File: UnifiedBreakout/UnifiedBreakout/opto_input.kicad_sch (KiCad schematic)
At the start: 5 parts, among them J17 RJ14, U3 4N35

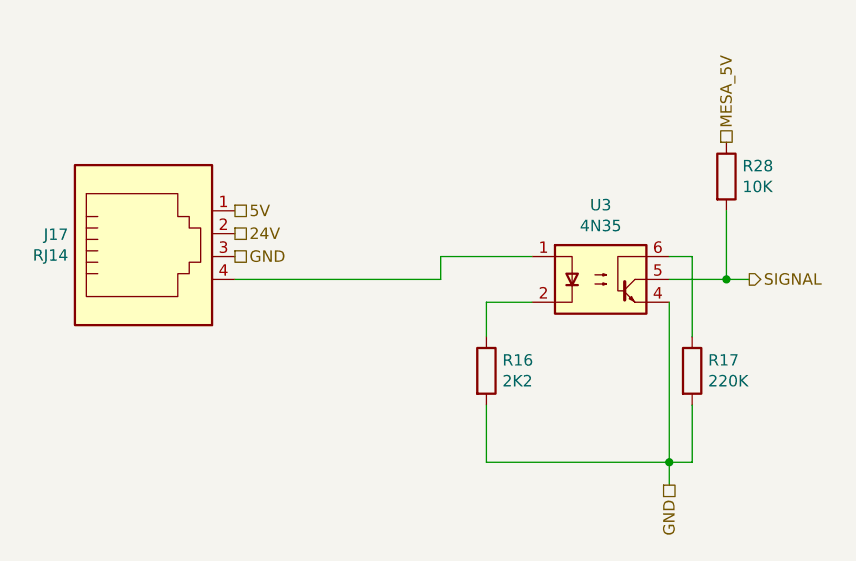
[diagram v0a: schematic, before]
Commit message: Upgrade to new KiCAD version
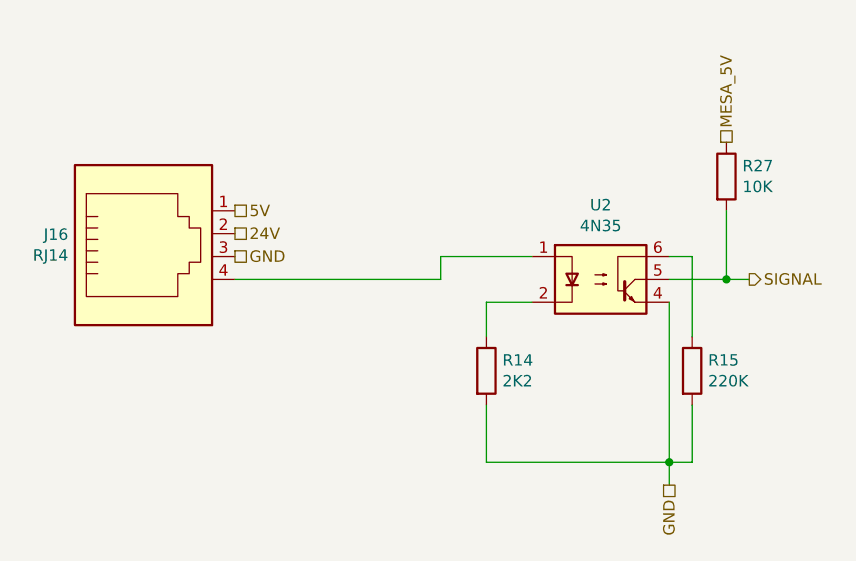
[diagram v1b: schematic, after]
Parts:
- renumbered J17 to J16, R16 to R14, R17 to R15, R28 to R27, U3 to U2
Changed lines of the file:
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@@
-(kicad_sch (version 20210126) (generator eeschema)
+(kicad_sch (version 20211123) (generator eeschema)
   (paper "A4")
-  (junction (at 153.67 109.22) (diameter 0.9144) (color 0 0 0 0))
-  (junction (at 160.02 88.9) (diameter 0.9144) (color 0 0 0 0))
-  (wire (pts (xy 105.41 88.9) (xy 128.27 88.9))
+  (junction (at 160.02 88.9) (diameter 0.9144) (color 0 0 0 0)
+  )
+  (junction (at 153.67 109.22) (diameter 0.9144) (color 0 0 0 0)
+  )
+  (wire (pts (xy 153.67 88.9) (xy 160.02 88.9))
     (stroke (width 0) (type solid) (color 0 0 0 0))
   )
-  (wire (pts (xy 128.27 86.36) (xy 138.43 86.36))
+  (wire (pts (xy 133.35 91.44) (xy 133.35 95.25))
+    (stroke (width 0) (type solid) (color 0 0 0 0))
+  )
+  (wire (pts (xy 156.21 86.36) (xy 156.21 95.25))
+    (stroke (width 0) (type solid) (color 0 0 0 0))
+  )
+  (wire (pts (xy 160.02 88.9) (xy 162.56 88.9))
     (stroke (width 0) (type solid) (color 0 0 0 0))
   )
@@
     (stroke (width 0) (type solid) (color 0 0 0 0))
   )
-  (wire (pts (xy 133.35 91.44) (xy 133.35 95.25))
+  (wire (pts (xy 138.43 91.44) (xy 133.35 91.44))
+    (stroke (width 0) (type solid) (color 0 0 0 0))
+  )
+  (wire (pts (xy 160.02 81.28) (xy 160.02 88.9))
+    (stroke (width 0) (type solid) (color 0 0 0 0))
+  )
+  (wire (pts (xy 156.21 102.87) (xy 156.21 109.22))
+    (stroke (width 0) (type solid) (color 0 0 0 0))
+  )
+  (wire (pts (xy 153.67 91.44) (xy 153.67 109.22))
     (stroke (width 0) (type solid) (color 0 0 0 0))
   )
@@
     (stroke (width 0) (type solid) (color 0 0 0 0))
   )
-  (wire (pts (xy 138.43 91.44) (xy 133.35 91.44))
-    (stroke (width 0) (type solid) (color 0 0 0 0))
-  )
-  (wire (pts (xy 153.67 86.36) (xy 156.21 86.36))
-    (stroke (width 0) (type solid) (color 0 0 0 0))
-  )
-  (wire (pts (xy 153.67 88.9) (xy 160.02 88.9))
-    (stroke (width 0) (type solid) (color 0 0 0 0))
-  )
-  (wire (pts (xy 153.67 91.44) (xy 153.67 109.22))
+  (wire (pts (xy 128.27 86.36) (xy 138.43 86.36))
     (stroke (width 0) (type solid) (color 0 0 0 0))
   )
@@
     (stroke (width 0) (type solid) (color 0 0 0 0))
   )
-  (wire (pts (xy 156.21 86.36) (xy 156.21 95.25))
-    (stroke (width 0) (type solid) (color 0 0 0 0))
-  )
-  (wire (pts (xy 156.21 102.87) (xy 156.21 109.22))
-    (stroke (width 0) (type solid) (color 0 0 0 0))
-  )
   (wire (pts (xy 156.21 109.22) (xy 153.67 109.22))
     (stroke (width 0) (type solid) (color 0 0 0 0))
   )
-  (wire (pts (xy 160.02 81.28) (xy 160.02 88.9))
+  (wire (pts (xy 153.67 86.36) (xy 156.21 86.36))
     (stroke (width 0) (type solid) (color 0 0 0 0))
   )
-  (wire (pts (xy 160.02 88.9) (xy 162.56 88.9))
+  (wire (pts (xy 105.41 88.9) (xy 128.27 88.9))
     (stroke (width 0) (type solid) (color 0 0 0 0))
+  )
+  (hierarchical_label "SIGNAL" (shape output) (at 162.56 88.9 0)
+    (effects (font (size 1.27 1.27)) (justify left))
+  )
+  (hierarchical_label "GND" (shape passive) (at 153.67 111.76 270)
+    (effects (font (size 1.27 1.27)) (justify right))
   )
   (hierarchical_label "5V" (shape passive) (at 105.41 81.28 0)
@@
     (effects (font (size 1.27 1.27)) (justify left))
   )
-  (hierarchical_label "GND" (shape passive) (at 153.67 111.76 270)
-    (effects (font (size 1.27 1.27)) (justify right))
-  )
   (hierarchical_label "MESA_5V" (shape passive) (at 160.02 73.66 90)
     (effects (font (size 1.27 1.27)) (justify left))
   )
-  (hierarchical_label "SIGNAL" (shape output) (at 162.56 88.9 0)
-    (effects (font (size 1.27 1.27)) (justify left))
+  (symbol (lib_id "UnifiedBreakout-rescue:R-Device") (at 160.02 77.47 0) (unit 1)
+    (in_bom yes) (on_board yes)
+    (property "Reference" "R27" (id 0) (at 161.798 76.3016 0)
+      (effects (font (size 1.27 1.27)) (justify left))
+    )
+    (property "Value" "10K" (id 1) (at 161.798 78.613 0)
+      (effects (font (size 1.27 1.27)) (justify left))
+    )
+    (property "Footprint" "Resistor_THT:R_Axial_DIN0207_L6.3mm_D2.5mm_P7.62mm_Horizontal" (id 2) (at 158.242 77.47 90)
+      (effects (font (size 1.27 1.27)) hide)
+    )
+    (property "Datasheet" "~" (id 3) (at 160.02 77.47 0)
+      (effects (font (size 1.27 1.27)) hide)
+    )
+    (property "MPN" "CFR-25JB-52-10K " (id 4) (at 160.02 77.47 0)
+      (effects (font (size 1.27 1.27)) hide)
+    )
+    (property "Manufacturer" "Yageo" (id 5) (at 160.02 77.47 0)
+      (effects (font (size 1.27 1.27)) hide)
+    )
+    (pin "1")
+    (pin "2")
   )
-  (symbol (lib_id "UnifiedBreakout-rescue:R-Device") (at 133.35 99.06 0)
+  (symbol (lib_id "UnifiedBreakout-rescue:4N35-Isolator") (at 146.05 88.9 0) (unit 1)
     (in_bom yes) (on_board yes)
-    (property "Reference" "R16" (id 0) (at 135.128 97.8916 0)
+    (property "Reference" "U2" (id 0) (at 146.05 80.645 0))
+    (property "Value" "4N35" (id 1) (at 146.05 82.9564 0))
+    (property "Footprint" "Package_DIP:DIP-6_W7.62mm" (id 2) (at 140.97 93.98 0)
+      (effects (font (size 1.27 1.27) italic) (justify left) hide)
+    )
+    (property "Datasheet" "https://www.vishay.com/docs/81181/4n35.pdf" (id 3) (at 146.05 88.9 0)
+      (effects (font (size 1.27 1.27)) (justify left) hide)
+    )
+    (property "MPN" "4N35" (id 4) (at 146.05 88.9 0)
+      (effects (font (size 1.27 1.27)) hide)
+    )
+    (property "Manufacturer" "Vishay" (id 5) (at 146.05 88.9 0)
+      (effects (font (size 1.27 1.27)) hide)
+    )
+    (pin "1")
+    (pin "2")
+    (pin "3")
+    (pin "4")
+    (pin "5")
+    (pin "6")
+  )
+  (symbol (lib_id "UnifiedBreakout-rescue:R-Device") (at 133.35 99.06 0) (unit 1)
+    (in_bom yes) (on_board yes)
+    (property "Reference" "R14" (id 0) (at 135.128 97.8916 0)
       (effects (font (size 1.27 1.27)) (justify left))
     )
@@
     (pin "2")
   )
-  (symbol (lib_id "UnifiedBreakout-rescue:R-Device") (at 156.21 99.06 0)
+  (symbol (lib_id "UnifiedBreakout-rescue:RJ14-Connector") (at 95.25 83.82 0) (mirror x) (unit 1)
     (in_bom yes) (on_board yes)
-    (property "Reference" "R17" (id 0) (at 157.988 97.8916 0)
-      (effects (font (size 1.27 1.27)) (justify left))
-    )
-    (property "Value" "220K" (id 1) (at 157.988 100.203 0)
-      (effects (font (size 1.27 1.27)) (justify left))
-    )
-    (property "Footprint" "Resistor_THT:R_Axial_DIN0207_L6.3mm_D2.5mm_P7.62mm_Horizontal" (id 2) (at 154.432 99.06 90)
-      (effects (font (size 1.27 1.27)) hide)
-    )
-    (property "Datasheet" "~" (id 3) (at 156.21 99.06 0)
-      (effects (font (size 1.27 1.27)) hide)
-    )
-    (property "MPN" "CFR-25JB-52-220K" (id 4) (at 156.21 99.06 0)
-      (effects (font (size 1.27 1.27)) hide)
-    )
-    (property "Manufacturer" "Yageo" (id 5) (at 156.21 99.06 0)
-      (effects (font (size 1.27 1.27)) hide)
-    )
-    (pin "1")
-    (pin "2")
-  )
-  (symbol (lib_id "UnifiedBreakout-rescue:R-Device") (at 160.02 77.47 0)
-    (in_bom yes) (on_board yes)
-    (property "Reference" "R28" (id 0) (at 161.798 76.3016 0)
-      (effects (font (size 1.27 1.27)) (justify left))
-    )
-    (property "Value" "10K" (id 1) (at 161.798 78.613 0)
-      (effects (font (size 1.27 1.27)) (justify left))
-    )
-    (property "Footprint" "Resistor_THT:R_Axial_DIN0207_L6.3mm_D2.5mm_P7.62mm_Horizontal" (id 2) (at 158.242 77.47 90)
-      (effects (font (size 1.27 1.27)) hide)
-    )
-    (property "Datasheet" "~" (id 3) (at 160.02 77.47 0)
-      (effects (font (size 1.27 1.27)) hide)
-    )
-    (property "MPN" "CFR-25JB-52-10K " (id 4) (at 160.02 77.47 0)
-      (effects (font (size 1.27 1.27)) hide)
-    )
-    (property "Manufacturer" "Yageo" (id 5) (at 160.02 77.47 0)
-      (effects (font (size 1.27 1.27)) hide)
-    )
-    (pin "1")
-    (pin "2")
-  )
-  (symbol (lib_id "UnifiedBreakout-rescue:4N35-Isolator") (at 146.05 88.9 0)
-    (in_bom yes) (on_board yes)
-    (property "Reference" "U3" (id 0) (at 146.05 80.645 0))
-    (property "Value" "4N35" (id 1) (at 146.05 82.9564 0))
-    (property "Footprint" "Package_DIP:DIP-6_W7.62mm" (id 2) (at 140.97 93.98 0)
-      (effects (font (size 1.27 1.27) italic) (justify left) hide)
-    )
-    (property "Datasheet" "https://www.vishay.com/docs/81181/4n35.pdf" (id 3) (at 146.05 88.9 0)
-      (effects (font (size 1.27 1.27)) (justify left) hide)
-    )
-    (property "MPN" "4N35" (id 4) (at 146.05 88.9 0)
-      (effects (font (size 1.27 1.27)) hide)
-    )
-    (property "Manufacturer" "Vishay" (id 5) (at 146.05 88.9 0)
-      (effects (font (size 1.27 1.27)) hide)
-    )
-    (pin "1")
-    (pin "2")
-    (pin "3")
-    (pin "4")
-    (pin "5")
-    (pin "6")
-  )
-  (symbol (lib_id "UnifiedBreakout-rescue:RJ14-Connector") (at 95.25 83.82 0) (mirror x)
-    (in_bom yes) (on_board yes)
-    (property "Reference" "J17" (id 0) (at 86.8934 83.9216 0)
+    (property "Reference" "J16" (id 0) (at 86.8934 83.9216 0)
       (effects (font (size 1.27 1.27)) (justify right))
     )
@@
     (pin "4")
   )
+  (symbol (lib_id "UnifiedBreakout-rescue:R-Device") (at 156.21 99.06 0) (unit 1)
+    (in_bom yes) (on_board yes)
+    (property "Reference" "R15" (id 0) (at 157.988 97.8916 0)
+      (effects (font (size 1.27 1.27)) (justify left))
+    )
+    (property "Value" "220K" (id 1) (at 157.988 100.203 0)
+      (effects (font (size 1.27 1.27)) (justify left))
+    )
+    (property "Footprint" "Resistor_THT:R_Axial_DIN0207_L6.3mm_D2.5mm_P7.62mm_Horizontal" (id 2) (at 154.432 99.06 90)
+      (effects (font (size 1.27 1.27)) hide)
+    )
+    (property "Datasheet" "~" (id 3) (at 156.21 99.06 0)
+      (effects (font (size 1.27 1.27)) hide)
+    )
+    (property "MPN" "CFR-25JB-52-220K" (id 4) (at 156.21 99.06 0)
+      (effects (font (size 1.27 1.27)) hide)
+    )
+    (property "Manufacturer" "Yageo" (id 5) (at 156.21 99.06 0)
+      (effects (font (size 1.27 1.27)) hide)
+    )
+    (pin "1")
+    (pin "2")
+  )
 )

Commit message: WIP updating breakout for electrical enclosure
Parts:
- removed J16: RJ14, Wurth:615004141121, symbol UnifiedBreakout-rescue:RJ14-Connector
- R14, R15, R27: symbol UnifiedBreakout-rescue:R-Device -> Device:R
- U2: symbol UnifiedBreakout-rescue:4N35-Isolator -> Isolator:4N35
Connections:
- net INPUT: now reaches U2.1

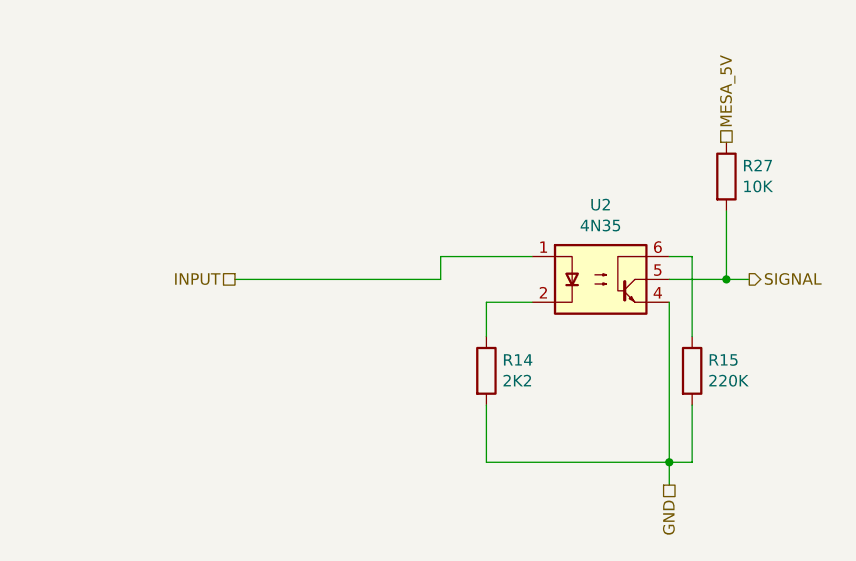
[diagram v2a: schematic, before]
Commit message: Update IO and opto
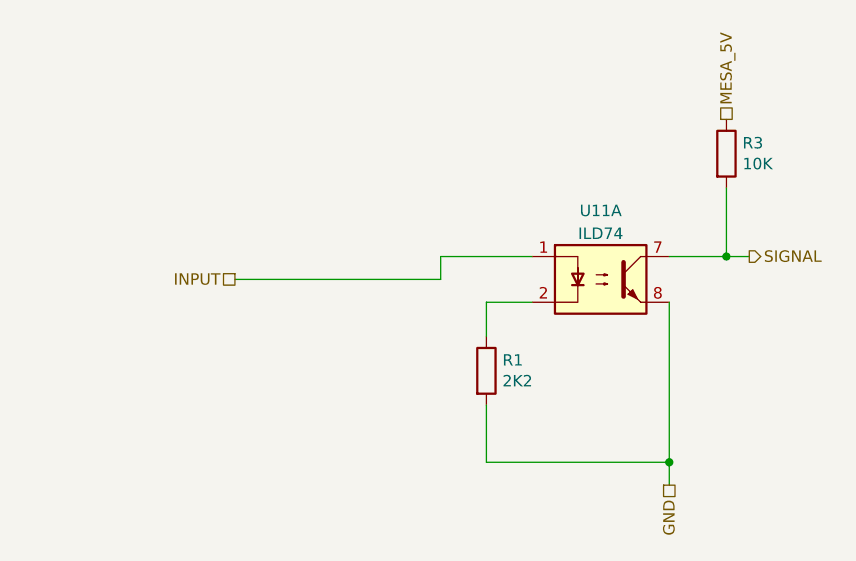
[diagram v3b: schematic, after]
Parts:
- removed R15: 220K, Resistor_THT:R_Axial_DIN0207_L6.3mm_D2.5mm_P7.62mm_Horizontal, symbol Device:R
- removed U2: 4N35, Package_DIP:DIP-6_W7.62mm, symbol Isolator:4N35
- added U11: ILD74, Package_DIP:DIP-8_W7.62mm_LongPads, symbol Isolator:ILD74
- renumbered R14 to R1, R27 to R3
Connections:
- net GND: now also U11.8
- net INPUT: now also U11.1
- net SIGNAL: now also U11.7
- net at R1.1: now also U11.2
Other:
- moved on the sheet: R3

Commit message: Started some layout
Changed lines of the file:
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@@
   (junction (at 160.02 86.36) (diameter 0.9144) (color 0 0 0 0)
   )
-  (junction (at 153.67 109.22) (diameter 0.9144) (color 0 0 0 0)
-  )
   (wire (pts (xy 153.67 86.36) (xy 160.02 86.36))
     (stroke (width 0) (type solid))
@@
     (stroke (width 0) (type solid))
   )
-  (wire (pts (xy 153.67 91.44) (xy 153.67 109.22))
+  (wire (pts (xy 153.67 91.44) (xy 153.67 111.76))
     (stroke (width 0) (type solid))
   )
@@
   )
   (wire (pts (xy 128.27 86.36) (xy 138.43 86.36))
-    (stroke (width 0) (type solid))
-  )
-  (wire (pts (xy 153.67 109.22) (xy 133.35 109.22))
-    (stroke (width 0) (type solid))
-  )
-  (wire (pts (xy 153.67 109.22) (xy 153.67 111.76))
     (stroke (width 0) (type solid))
   )
@@
         )
       )
+    )
+  )
+  (symbol (lib_id "power:GND") (at 133.35 109.22 0) (unit 1)
+    (in_bom yes) (on_board yes) (dnp no) (fields_autoplaced)
+    (property "Reference" "#PWR045" (at 133.35 114.3 0)
+      (effects (font (size 1.27 1.27)) hide)
+    )
+    (property "Value" "GNDPWR" (at 133.223 114.3 0)
+      (effects (font (size 1.27 1.27)))
+    )
+    (property "Footprint" "" (at 133.35 109.22 0)
+      (effects (font (size 1.27 1.27)) hide)
+    )
+    (property "Datasheet" "" (at 133.35 109.22 0)
+      (effects (font (size 1.27 1.27)) hide)
+    )
+    (pin "1")
+    (instances
+      (project "UnifiedBreakout"
+        (path "/e63e39d7-6ac0-4ffd-8aa3-1841a4541b55/00000000-0000-0000-0000-00005ea83ccc"
+          (reference "#PWR045") (unit 1)
+        )
+        (path "/e63e39d7-6ac0-4ffd-8aa3-1841a4541b55/00000000-0000-0000-0000-00005ea623ae"
+          (reference "#PWR043") (unit 1)
+        )
+        (path "/e63e39d7-6ac0-4ffd-8aa3-1841a4541b55/00000000-0000-0000-0000-00005ea86618"
+          (reference "#PWR044") (unit 1)
+        )
+        (path "/e63e39d7-6ac0-4ffd-8aa3-1841a4541b55/00000000-0000-0000-0000-00005ea816c6"
+          (reference "#PWR046") (unit 1)
+        )
+        (path "/e63e39d7-6ac0-4ffd-8aa3-1841a4541b55/00000000-0000-0000-0000-00005ea7f263"
+          (reference "#PWR047") (unit 1)
+        )
+        (path "/e63e39d7-6ac0-4ffd-8aa3-1841a4541b55/a961b421-d2a6-477a-a4b0-5977252d73f9"
+          (reference "#PWR048") (unit 1)
+        )
+      )

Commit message: Some layout
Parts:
- renumbered R3 to R2, U11 to U1
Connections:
- net GND: now also U1.5; no longer U1.8
- net INPUT: now also U1.4; no longer U1.1
- net SIGNAL: now also U1.6; no longer U1.7
- net at R1.1: now also U1.3; no longer U1.2
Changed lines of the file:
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@@
   (symbol (lib_id "Device:R") (at 160.02 74.93 0) (unit 1)
     (in_bom yes) (on_board yes) (dnp no)
-    (property "Reference" "R3" (at 161.798 73.7616 0)
+    (property "Reference" "R2" (at 161.798 73.7616 0)
       (effects (font (size 1.27 1.27)) (justify left))
     )
@@
       (project "UnifiedBreakout"
         (path "/e63e39d7-6ac0-4ffd-8aa3-1841a4541b55/00000000-0000-0000-0000-00005ea623ae"
-          (reference "R3") (unit 1)
+          (reference "R2") (unit 1)
         )
         (path "/e63e39d7-6ac0-4ffd-8aa3-1841a4541b55/00000000-0000-0000-0000-00005ea7f263"
-          (reference "R15") (unit 1)
+          (reference "R10") (unit 1)
         )
         (path "/e63e39d7-6ac0-4ffd-8aa3-1841a4541b55/00000000-0000-0000-0000-00005ea816c6"
-          (reference "R12") (unit 1)
+          (reference "R8") (unit 1)
         )
         (path "/e63e39d7-6ac0-4ffd-8aa3-1841a4541b55/00000000-0000-0000-0000-00005ea83ccc"
-          (reference "R9") (unit 1)
+          (reference "R6") (unit 1)
         )
         (path "/e63e39d7-6ac0-4ffd-8aa3-1841a4541b55/00000000-0000-0000-0000-00005ea86618"
-          (reference "R6") (unit 1)
+          (reference "R4") (unit 1)
         )
         (path "/e63e39d7-6ac0-4ffd-8aa3-1841a4541b55/a961b421-d2a6-477a-a4b0-5977252d73f9"
-          (reference "R25") (unit 1)
+          (reference "R20") (unit 1)
         )
       )
@@
         )
         (path "/e63e39d7-6ac0-4ffd-8aa3-1841a4541b55/00000000-0000-0000-0000-00005ea7f263"
-          (reference "R13") (unit 1)
+          (reference "R9") (unit 1)
         )
         (path "/e63e39d7-6ac0-4ffd-8aa3-1841a4541b55/00000000-0000-0000-0000-00005ea816c6"
-          (reference "R10") (unit 1)
+          (reference "R7") (unit 1)
         )
         (path "/e63e39d7-6ac0-4ffd-8aa3-1841a4541b55/00000000-0000-0000-0000-00005ea83ccc"
-          (reference "R7") (unit 1)
+          (reference "R5") (unit 1)
         )
         (path "/e63e39d7-6ac0-4ffd-8aa3-1841a4541b55/00000000-0000-0000-0000-00005ea86618"
-          (reference "R4") (unit 1)
+          (reference "R3") (unit 1)
         )
         (path "/e63e39d7-6ac0-4ffd-8aa3-1841a4541b55/a961b421-d2a6-477a-a4b0-5977252d73f9"
-          (reference "R23") (unit 1)
+          (reference "R19") (unit 1)
         )
       )
     )
   )
-  (symbol (lib_id "Isolator:ILD74") (at 146.05 88.9 0) (unit 1)
+  (symbol (lib_id "Isolator:ILD74") (at 146.05 88.9 0) (unit 2)
     (in_bom yes) (on_board yes) (dnp no) (fields_autoplaced)
-    (property "Reference" "U11" (at 146.05 81.28 0)
+    (property "Reference" "U1" (at 146.05 81.28 0)
       (effects (font (size 1.27 1.27)))
     )
@@
       (project "UnifiedBreakout"
         (path "/e63e39d7-6ac0-4ffd-8aa3-1841a4541b55/00000000-0000-0000-0000-00005ea623ae"
-          (reference "U11") (unit 1)
+          (reference "U1") (unit 2)
         )
         (path "/e63e39d7-6ac0-4ffd-8aa3-1841a4541b55/00000000-0000-0000-0000-00005ea86618"
-          (reference "U13") (unit 2)
+          (reference "U1") (unit 1)
         )
         (path "/e63e39d7-6ac0-4ffd-8aa3-1841a4541b55/00000000-0000-0000-0000-00005ea83ccc"
-          (reference "U12") (unit 2)
+          (reference "U2") (unit 1)
         )
         (path "/e63e39d7-6ac0-4ffd-8aa3-1841a4541b55/00000000-0000-0000-0000-00005ea816c6"
-          (reference "U12") (unit 1)
+          (reference "U3") (unit 2)
         )
         (path "/e63e39d7-6ac0-4ffd-8aa3-1841a4541b55/00000000-0000-0000-0000-00005ea7f263"
-          (reference "U11") (unit 2)
+          (reference "U3") (unit 1)
         )
         (path "/e63e39d7-6ac0-4ffd-8aa3-1841a4541b55/a961b421-d2a6-477a-a4b0-5977252d73f9"
-          (reference "U13") (unit 1)
+          (reference "U2") (unit 2)
         )
       )
@@
   (symbol (lib_id "power:GND") (at 133.35 109.22 0) (unit 1)
     (in_bom yes) (on_board yes) (dnp no) (fields_autoplaced)
-    (property "Reference" "#PWR045" (at 133.35 114.3 0)
+    (property "Reference" "#PWR03" (at 133.35 114.3 0)
       (effects (font (size 1.27 1.27)) hide)
     )
@@
       (project "UnifiedBreakout"
         (path "/e63e39d7-6ac0-4ffd-8aa3-1841a4541b55/00000000-0000-0000-0000-00005ea83ccc"
-          (reference "#PWR045") (unit 1)
+          (reference "#PWR03") (unit 1)
         )
         (path "/e63e39d7-6ac0-4ffd-8aa3-1841a4541b55/00000000-0000-0000-0000-00005ea623ae"
-          (reference "#PWR043") (unit 1)
+          (reference "#PWR01") (unit 1)
         )
         (path "/e63e39d7-6ac0-4ffd-8aa3-1841a4541b55/00000000-0000-0000-0000-00005ea86618"
-          (reference "#PWR044") (unit 1)
+          (reference "#PWR02") (unit 1)
         )
         (path "/e63e39d7-6ac0-4ffd-8aa3-1841a4541b55/00000000-0000-0000-0000-00005ea816c6"
-          (reference "#PWR046") (unit 1)
+          (reference "#PWR04") (unit 1)
         )
         (path "/e63e39d7-6ac0-4ffd-8aa3-1841a4541b55/00000000-0000-0000-0000-00005ea7f263"
-          (reference "#PWR047") (unit 1)
+          (reference "#PWR05") (unit 1)
         )
         (path "/e63e39d7-6ac0-4ffd-8aa3-1841a4541b55/a961b421-d2a6-477a-a4b0-5977252d73f9"
